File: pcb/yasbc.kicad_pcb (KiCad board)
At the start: 4 copper layers, 183 parts, among them J1 BOOT, J10 SSD1309, J2 USB TTY, J3 AudioJack3, J4 1V5, J5 3V3, J6 1V2, J7 USB DEV, J8 Micro_SD_Card, J9 USB HOST, Q1 AO3401A, Q2 AO3401A, SW1 RESET, SW2 SW_SPDT, SW3 SW_SPDT, SW4 SW_SPDT, SW5 SW_SPDT, SW6 SW_5WAY, U1 BCT2028, U2 ESP32-WROOM-32, U3 Allwinner_A13, U4 CH340E, U5 TD6810, U6 SE5120, U7 MT3608, U8 K4B4G1646E, U9 MPU-6050, Y1 24M

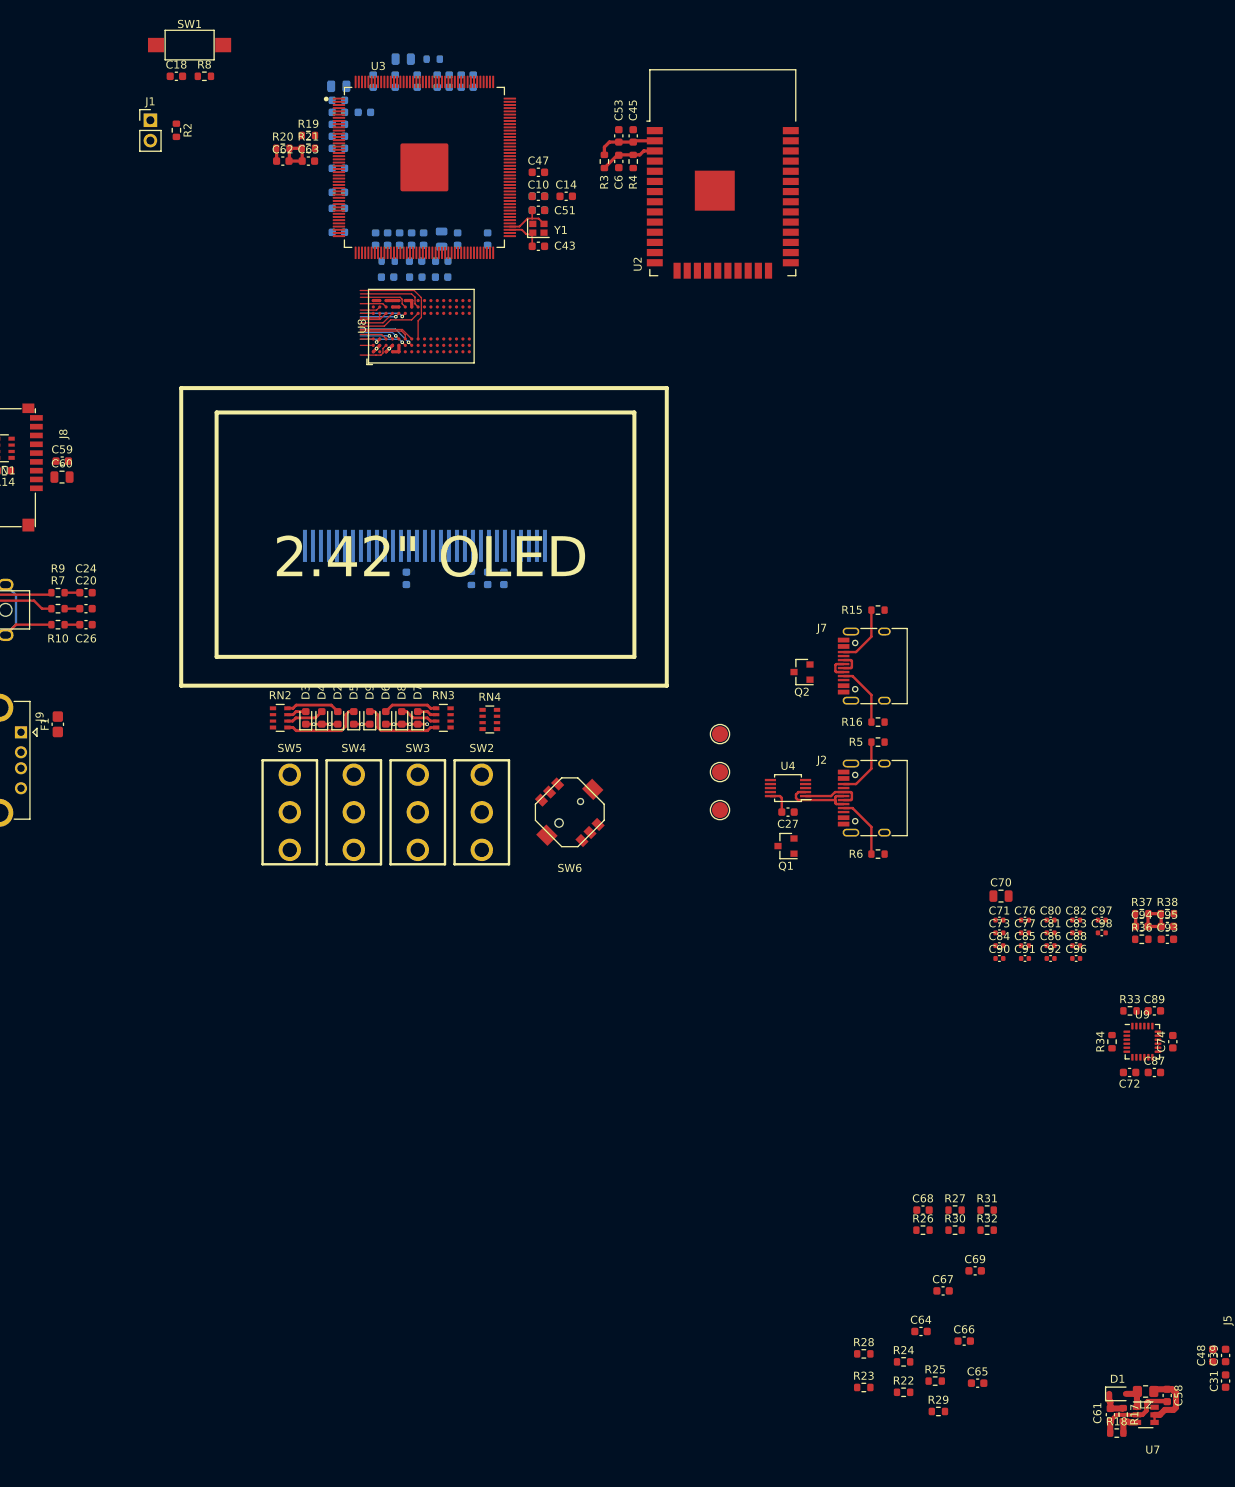
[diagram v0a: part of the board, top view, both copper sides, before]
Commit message: Removed OLED and ESP32
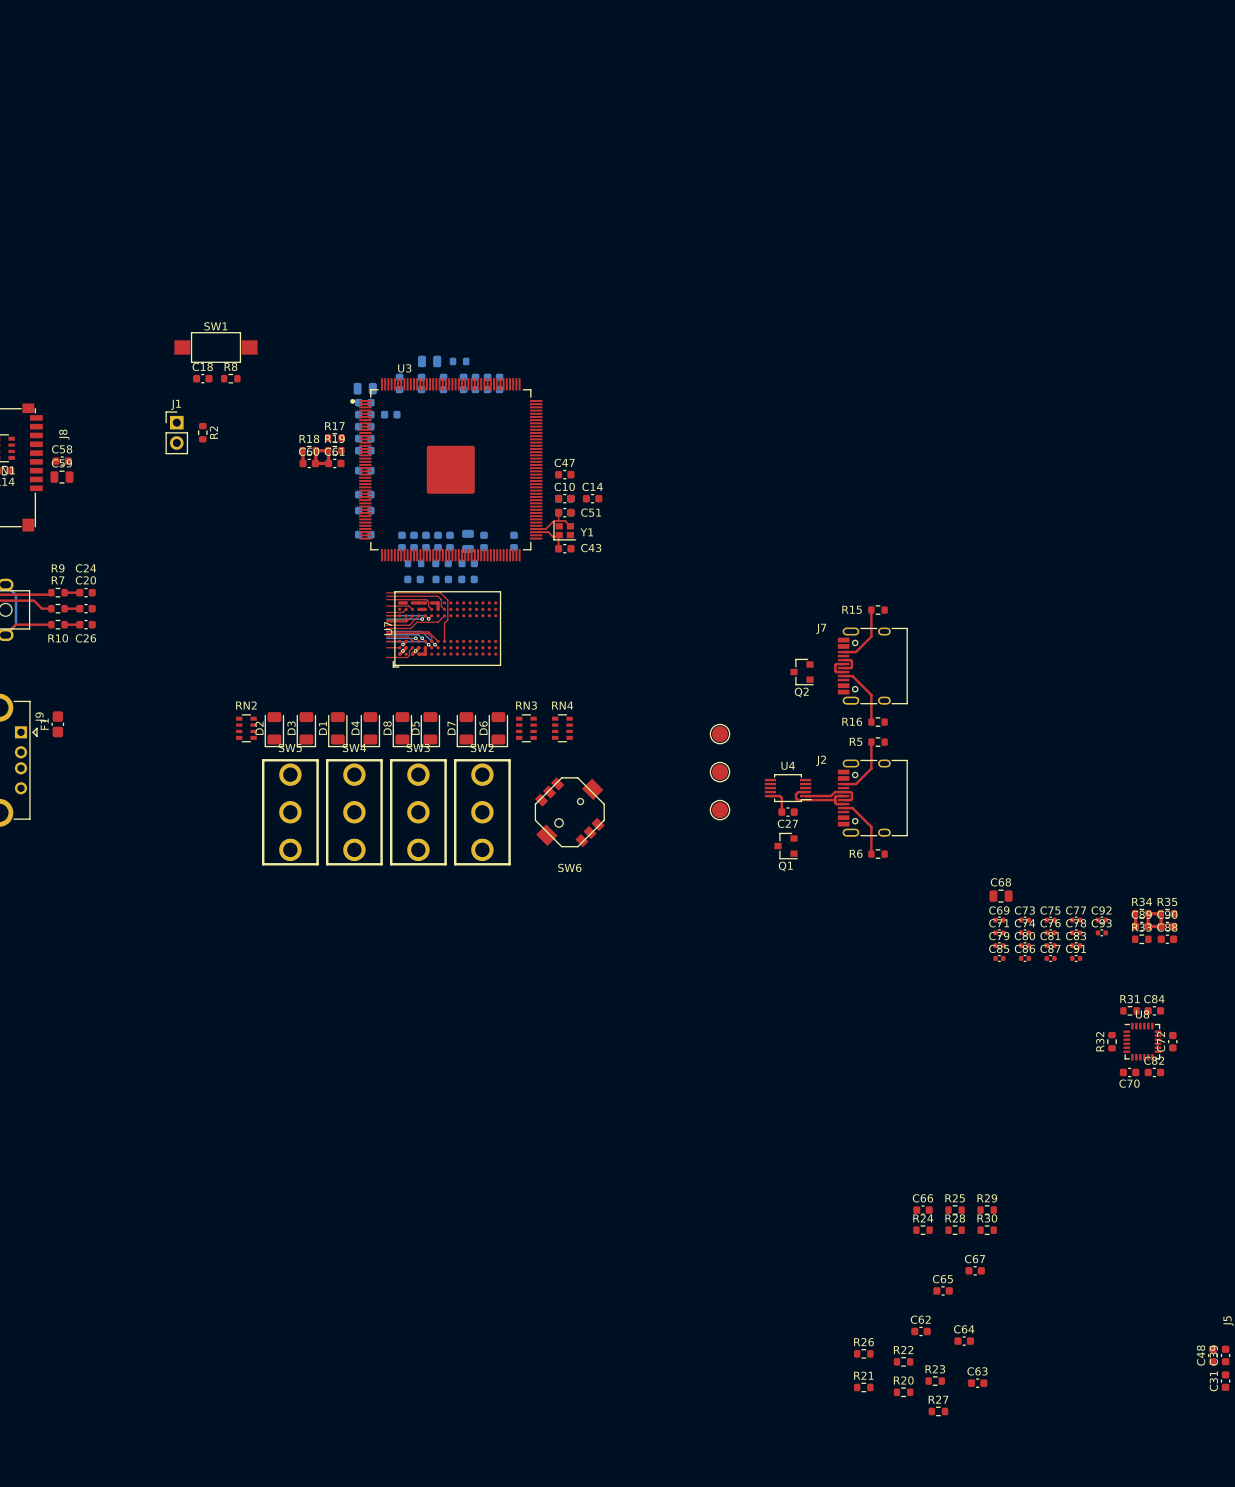
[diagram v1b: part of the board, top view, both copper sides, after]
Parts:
- removed C45: 0.1u, Capacitor_SMD:C_0603_1608Metric
- removed C53: 10u, Capacitor_SMD:C_0603_1608Metric
- removed the C58 at (205.1, 152.0)
- removed C6: DNF, Capacitor_SMD:C_0603_1608Metric
- removed the C61 at (198.0, 154.4)
- removed the C75 at (120.2, 49.9)
- removed the C78 at (122.2, 49.9)
- removed the C79 at (110.0, 49.9)
- removed the D1 at (198.9, 151.8)
- removed the D3 at (97.4, 67.3)
- removed J10: SSD1309, yasbc:SSD1309
- removed L2: 4.7u, Inductor_SMD:L_0805_2012Metric_Pad1.15x1.40mm_HandSolder
- removed the R17 at (199.6, 154.4)
- removed the R18 at (198.8, 156.7)
- removed R3: DNF, Resistor_SMD:R_0603_1608Metric
- removed the R35 at (118.1, 49.9)
- removed R4: 10K, Resistor_SMD:R_0603_1608Metric
- removed U2: ESP32-WROOM-32, RF_Module:ESP32-WROOM-32
- removed the U7 at (202.4, 154.4)
- added D2: LED_Small, LED_SMD:LED_1206_3216Metric, F.Cu at (93.5, 68.6)
- D1: renamed from D2; footprint LED_SMD:LED_0603_1608Metric -> LED_SMD:LED_1206_3216Metric
- D3: renamed from D4; footprint LED_SMD:LED_0603_1608Metric -> LED_SMD:LED_1206_3216Metric
- D4: renamed from D5; footprint LED_SMD:LED_0603_1608Metric -> LED_SMD:LED_1206_3216Metric
- D5: renamed from D6; footprint LED_SMD:LED_0603_1608Metric -> LED_SMD:LED_1206_3216Metric
- D6: renamed from D7; footprint LED_SMD:LED_0603_1608Metric -> LED_SMD:LED_1206_3216Metric
- D7: renamed from D8; footprint LED_SMD:LED_0603_1608Metric -> LED_SMD:LED_1206_3216Metric
- D8: renamed from D9; footprint LED_SMD:LED_0603_1608Metric -> LED_SMD:LED_1206_3216Metric
- moved U3 37.9 mm to (115.5, 36.3)
- moved C10 37.9 mm to (129.8, 39.9)
- moved C11 37.9 mm to (114.7, 25.5)
- moved C12 37.9 mm to (109.2, 25.5)
- moved C13 37.9 mm to (118.7, 25.5)
- moved C14 37.9 mm to (133.3, 39.9)
- moved C15 37.9 mm to (104.8, 29.4)
- moved C16 37.9 mm to (120.2, 25.5)
- moved C17 37.9 mm to (114.0, 45.2)
- moved C18 37.9 mm to (84.5, 24.9)
- moved C2 37.9 mm to (104.8, 26.1)
- moved C21 37.9 mm to (117.2, 25.5)
- moved C22 37.9 mm to (121.7, 25.5)
- moved C23 37.9 mm to (129.8, 41.6)
- moved C28 37.9 mm to (117.7, 48.0)
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- renumbered C59 to C58, C60 to C59, C62 to C60, C63 to C61, C64 to C62, C65 to C63, C66 to C64, C67 to C65, C68 to C66, C69 to C67, C70 to C68, C71 to C69, C72 to C70, C73 to C71, C74 to C72, C76 to C73, C77 to C74, C80 to C75, C81 to C76, C82 to C77, C83 to C78, C84 to C79, C85 to C80, C86 to C81, C87 to C82, C88 to C83, C89 to C84, C90 to C85, C91 to C86, C92 to C87, C93 to C88, C94 to C89, C95 to C90, C96 to C91, C97 to C92, C98 to C93, R19 to R17, R20 to R18, R21 to R19, R22 to R20, R23 to R21, R24 to R22, R25 to R23, R26 to R24, R27 to R25, R28 to R26, R29 to R27, R30 to R28, R31 to R29, R32 to R30, R33 to R31, R34 to R32, R36 to R33, R37 to R34, R38 to R35, U8 to U7, U9 to U8
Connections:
- U3 pad 1: /OLED_DC -> Net-(U3-Pad1)
- U3 pad 12: /ESP_RX -> Net-(U3-Pad12)
- U3 pad 13: /ESP_TX -> Net-(U3-Pad13)
- U3 pad 14: /ESP_RTS -> Net-(U3-Pad14)
- U3 pad 15: /ESP_CTS -> Net-(U3-Pad15)
- U3 pad 153: /ESP_EN -> Net-(U3-Pad153)
- U3 pad 162: /ESP_BOOT -> Net-(U3-Pad162)
- U3 pad 170: /ESP_DAT3 -> Net-(U3-Pad170)
- U3 pad 171: /ESP_DAT2 -> Net-(U3-Pad171)
- U3 pad 172: /ESP_DAT1 -> Net-(U3-Pad172)
- U3 pad 174: /ESP_DAT0 -> Net-(U3-Pad174)
- U3 pad 175: /ESP_CLK -> Net-(U3-Pad175)
- U3 pad 176: /ESP_CMD -> Net-(U3-Pad176)
- U3 pad 2: /OLED_RES -> Net-(U3-Pad2)
- U3 pad 3: /OLED_CS -> Net-(U3-Pad3)
- U3 pad 6: /OLED_SCLK -> Net-(U3-Pad6)
- U3 pad 8: /OLED_SDIN -> Net-(U3-Pad8)
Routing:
- net GND: track 44.1 -> 22.4 mm, vias 7 -> 1
- net Net-(D8-Pad2): track 10.4 -> 0.00 mm
- net Net-(D4-Pad2): track 10.3 -> 0.00 mm
- net VBUS: track 16.9 -> 8.00 mm
- net +3V3: track 10.9 -> 3.29 mm
- net /ESP_EN: track 7.19 -> 0.00 mm
- net Net-(D1-Pad2): track 6.80 -> 0.00 mm
- net Net-(D5-Pad2): track 6.80 -> 0.00 mm
- net Net-(D3-Pad2): track 4.79 -> 0.00 mm
- net Net-(D7-Pad2): track 4.79 -> 0.00 mm
- net Net-(D1-Pad2) (its old number): track 3.54 -> 0.00 mm
- net +12V: track 3.51 -> 0.00 mm
- net Net-(R17-Pad2): track 3.01 -> 0.00 mm
- net Net-(D2-Pad2): track 2.46 -> 0.00 mm
- net Net-(D6-Pad2): track 2.46 -> 0.00 mm
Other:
- board text removed: "2.42" OLED"

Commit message: Converted to kicad 6 and worked on pcb
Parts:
- added D9: 5V, Diode_SMD:D_SMB, F.Cu at (134.5, 143.4)
- added H1: MountingHole, MountingHole:MountingHole_3.2mm_M3, F.Cu at (132.5, -105.5)
- added H2: MountingHole, MountingHole:MountingHole_3.2mm_M3, F.Cu at (132.5, -14.5)
- added H3: MountingHole, MountingHole:MountingHole_3.2mm_M3, F.Cu at (41.5, -105.5)
- added H4: MountingHole, MountingHole:MountingHole_3.2mm_M3, F.Cu at (41.5, -14.5)
- added J10: Conn_02x20_Odd_Even, Connector_PinHeader_2.54mm:PinHeader_2x20_P2.54mm_Vertical, F.Cu at (47.0, -105.0)
- added R3: 5.1K, Resistor_SMD:R_0603_1608Metric, F.Cu at (159.6, 141.3)
- added R4: 5.1K, Resistor_SMD:R_0603_1608Metric, F.Cu at (163.6, 141.3)
- C10, C14, C47, C60, C61, R17, R18, R19: moved to B.Cu
- moved R6 226.2 mm to (12.6, -79.1), turned to 180 degrees
- moved J2 215.9 mm to (12.8, -72.1), turned to -90 degrees
- moved Q1 209.4 mm to (24.1, -78.1), turned to 0 degrees
- moved R5 206.9 mm to (12.6, -65.1), turned to 180 degrees
- moved U7 204.6 mm to (-51.6, -62.5), turned to 45 degrees
- moved C27 203.2 mm to (23.8, -73.8), turned to 180 degrees
- moved C23 199.8 mm to (-31.2, -76.6)
- moved U4 198.8 mm to (23.8, -70.8), turned to 0 degrees
- moved C14 198.0 mm to (-27.8, -75.3)
- moved C10 198.0 mm to (-31.3, -75.3)
- moved TP1 196.7 mm to (30.0, -77.7), turned to 0 degrees
- moved C47 194.9 mm to (-31.3, -72.9)
- moved C42 194.1 mm to (-27.8, -73.3), turned to 180 degrees
- moved R17 191.2 mm to (-53.9, -79.9), turned to -90 degrees
- moved R19 190.9 mm to (-52.2, -79.9), turned to -90 degrees
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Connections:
- U3 pad 10: /SW_RIGHT -> /SPI2_CS1
- U3 pad 103: /SW_UP -> Net-(U3-Pad103)
- U3 pad 104: /SW_LEFT -> Net-(U3-Pad104)
- U3 pad 105: /LED5 -> Net-(U3-Pad105)
- U3 pad 106: /LED6 -> Net-(U3-Pad106)
- U3 pad 114: Net-(U3-Pad114) -> /SPI2_CS0
- U3 pad 115: Net-(U3-Pad115) -> /SPI2_CLK
- U3 pad 116: Net-(U3-Pad116) -> /SPI2_MOSI
- U3 pad 117: Net-(U3-Pad117) -> /SPI2_MISO
- U3 pad 118: Net-(U3-Pad118) -> /SDC2_DAT0
- U3 pad 119: Net-(U3-Pad119) -> /SDC2_DAT1
- U3 pad 120: Net-(U3-Pad120) -> /SDC2_DAT2
- U3 pad 121: Net-(U3-Pad121) -> /SDC2_DAT3
- U3 pad 122: Net-(U3-Pad122) -> /SDC2_CMD
- U3 pad 123: Net-(U3-Pad123) -> /SDC2_CLK
- U3 pad 150: /SW_DOWN -> Net-(U3-Pad150)
- U3 pad 160: /LED8 -> Net-(U3-Pad160)
- U3 pad 161: /LED7 -> Net-(U3-Pad161)
- U3 pad 165: /LED4 -> /LED8
- U3 pad 166: /LED3 -> /LED7
- U3 pad 167: /LED2 -> /LED6
- U3 pad 168: /LED1 -> /LED5
- U3 pad 170: Net-(U3-Pad170) -> /LED4
- U3 pad 171: Net-(U3-Pad171) -> /LED3
- U3 pad 172: Net-(U3-Pad172) -> /LED2
- U3 pad 174: Net-(U3-Pad174) -> /LED1
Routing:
- net /DDR3_D4: track 13.4 -> 0.00 mm
- net /DDR3_DQS1-: track 2.97 -> 14.7 mm
- net /DDR3_DQS1+: track 3.56 -> 14.8 mm
- net /DDR3_CK-: track 0.00 -> 10.6 mm, vias 0 -> 2
- net /DDR3_DQS0+: track 6.35 -> 16.8 mm, vias 0 -> 2
- net /DDR3_CK+: track 0.00 -> 10.3 mm, vias 0 -> 2
- net /DDR3_DQS0-: track 6.93 -> 16.4 mm, vias 0 -> 2
- net /DDR3_D0: track 5.18 -> 14.5 mm
- net /DDR3_D6: track 7.28 -> 16.4 mm
- net /DDR3_D12: track 1.63 -> 10.7 mm
- net /DDR3_DM0: track 5.00 -> 13.7 mm, vias 1 -> 2
- net /DDR3_D8: track 4.55 -> 11.8 mm
- net /DDR3_D14: track 2.60 -> 8.94 mm
- net /DDR3_D2: track 5.95 -> 0.00 mm, vias 1 -> 0
- net /DDR3_D10: track 3.41 -> 8.44 mm
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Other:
- board outline added: 100 x 100 mm
- net class DDR3 removed
- net class Default removed
- board text added: "JLC2313 1.6mm"

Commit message: Routed DDR3 data signals
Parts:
- moved C10 119.4 mm to (86.0, -52.7)
- moved C11 119.4 mm to (80.7, -66.6)
- moved C12 119.4 mm to (75.2, -66.6)
- moved C13 119.4 mm to (84.7, -66.6)
- moved C16 119.4 mm to (86.2, -66.6)
- moved C21 119.4 mm to (83.2, -66.6)
- moved C22 119.4 mm to (87.7, -66.6)
- moved C23 119.4 mm to (86.1, -54.0)
- moved C42 119.4 mm to (89.5, -50.8)
- moved C43 119.4 mm to (94.8, -45.3)
- moved C47 119.4 mm to (86.0, -50.3)
- moved C50 119.4 mm to (77.9, -66.6)
- moved C51 119.4 mm to (96.9, -47.2)
- moved C55 119.4 mm to (78.9, -69.3)
- moved R11 119.4 mm to (82.7, -69.3)
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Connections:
- J10 pad 11: Net-(J10-Pad11) -> unconnected-(J10-Pad11)
- J10 pad 12: Net-(J10-Pad12) -> unconnected-(J10-Pad12)
- J10 pad 27: Net-(J10-Pad27) -> unconnected-(J10-Pad27)
- J10 pad 28: Net-(J10-Pad28) -> unconnected-(J10-Pad28)
- J10 pad 29: Net-(J10-Pad29) -> unconnected-(J10-Pad29)
- J10 pad 31: Net-(J10-Pad31) -> unconnected-(J10-Pad31)
- J10 pad 32: Net-(J10-Pad32) -> unconnected-(J10-Pad32)
- J10 pad 33: Net-(J10-Pad33) -> unconnected-(J10-Pad33)
- J10 pad 35: Net-(J10-Pad35) -> unconnected-(J10-Pad35)
- J10 pad 36: Net-(J10-Pad36) -> unconnected-(J10-Pad36)
- J10 pad 38: Net-(J10-Pad38) -> unconnected-(J10-Pad38)
- J10 pad 40: Net-(J10-Pad40) -> unconnected-(J10-Pad40)
- J10 pad 7: Net-(J10-Pad7) -> unconnected-(J10-Pad7)
- J2 pad A8: Net-(J2-PadA8) -> unconnected-(J2-PadA8)
- J2 pad B8: Net-(J2-PadB8) -> unconnected-(J2-PadB8)
- J7 pad A8: Net-(J7-PadA8) -> unconnected-(J7-PadA8)
- J7 pad B8: Net-(J7-PadB8) -> unconnected-(J7-PadB8)
- U3 pad 1: Net-(U3-Pad1) -> unconnected-(U3-Pad1)
- U3 pad 103: Net-(U3-Pad103) -> unconnected-(U3-Pad103)
- U3 pad 104: Net-(U3-Pad104) -> unconnected-(U3-Pad104)
- U3 pad 105: Net-(U3-Pad105) -> unconnected-(U3-Pad105)
- U3 pad 106: Net-(U3-Pad106) -> unconnected-(U3-Pad106)
- U3 pad 12: Net-(U3-Pad12) -> unconnected-(U3-Pad12)
- U3 pad 124: Net-(U3-Pad124) -> unconnected-(U3-Pad124)
- U3 pad 125: Net-(U3-Pad125) -> unconnected-(U3-Pad125)
- U3 pad 126: Net-(U3-Pad126) -> unconnected-(U3-Pad126)
- U3 pad 127: Net-(U3-Pad127) -> unconnected-(U3-Pad127)
- U3 pad 128: Net-(U3-Pad128) -> unconnected-(U3-Pad128)
- U3 pad 129: Net-(U3-Pad129) -> unconnected-(U3-Pad129)
- U3 pad 13: Net-(U3-Pad13) -> unconnected-(U3-Pad13)
- U3 pad 130: Net-(U3-Pad130) -> unconnected-(U3-Pad130)
- U3 pad 131: Net-(U3-Pad131) -> unconnected-(U3-Pad131)
- U3 pad 132: Net-(U3-Pad132) -> unconnected-(U3-Pad132)
- U3 pad 133: Net-(U3-Pad133) -> unconnected-(U3-Pad133)
- U3 pad 134: Net-(U3-Pad134) -> unconnected-(U3-Pad134)
- U3 pad 135: Net-(U3-Pad135) -> unconnected-(U3-Pad135)
- U3 pad 136: Net-(U3-Pad136) -> unconnected-(U3-Pad136)
- U3 pad 137: Net-(U3-Pad137) -> unconnected-(U3-Pad137)
- U3 pad 138: Net-(U3-Pad138) -> unconnected-(U3-Pad138)
- U3 pad 139: Net-(U3-Pad139) -> unconnected-(U3-Pad139)
- U3 pad 14: Net-(U3-Pad14) -> unconnected-(U3-Pad14)
- U3 pad 140: Net-(U3-Pad140) -> unconnected-(U3-Pad140)
- U3 pad 141: Net-(U3-Pad141) -> unconnected-(U3-Pad141)
- U3 pad 143: Net-(U3-Pad143) -> unconnected-(U3-Pad143)
- U3 pad 144: Net-(U3-Pad144) -> unconnected-(U3-Pad144)
- U3 pad 145: Net-(U3-Pad145) -> unconnected-(U3-Pad145)
- U3 pad 146: Net-(U3-Pad146) -> unconnected-(U3-Pad146)
- U3 pad 147: Net-(U3-Pad147) -> unconnected-(U3-Pad147)
- U3 pad 148: Net-(U3-Pad148) -> unconnected-(U3-Pad148)
- U3 pad 15: Net-(U3-Pad15) -> unconnected-(U3-Pad15)
- U3 pad 150: Net-(U3-Pad150) -> unconnected-(U3-Pad150)
- U3 pad 153: Net-(U3-Pad153) -> unconnected-(U3-Pad153)
- U3 pad 160: Net-(U3-Pad160) -> unconnected-(U3-Pad160)
- U3 pad 161: Net-(U3-Pad161) -> unconnected-(U3-Pad161)
- U3 pad 162: Net-(U3-Pad162) -> unconnected-(U3-Pad162)
- U3 pad 175: Net-(U3-Pad175) -> unconnected-(U3-Pad175)
- U3 pad 176: Net-(U3-Pad176) -> unconnected-(U3-Pad176)
- U3 pad 2: Net-(U3-Pad2) -> unconnected-(U3-Pad2)
- U3 pad 3: Net-(U3-Pad3) -> unconnected-(U3-Pad3)
- U3 pad 6: Net-(U3-Pad6) -> unconnected-(U3-Pad6)
- U3 pad 7: Net-(U3-Pad7) -> unconnected-(U3-Pad7)
- U3 pad 8: Net-(U3-Pad8) -> unconnected-(U3-Pad8)
- U3 pad 84: Net-(U3-Pad84) -> unconnected-(U3-Pad84)
- U3 pad 85: Net-(U3-Pad85) -> unconnected-(U3-Pad85)
- U3 pad 87: Net-(U3-Pad87) -> unconnected-(U3-Pad87)
- U3 pad 88: Net-(U3-Pad88) -> unconnected-(U3-Pad88)
- U3 pad 89: Net-(U3-Pad89) -> unconnected-(U3-Pad89)
- U3 pad 90: Net-(U3-Pad90) -> unconnected-(U3-Pad90)
- U3 pad 99: Net-(U3-Pad99) -> unconnected-(U3-Pad99)
- U4 pad 4: Net-(U4-Pad4) -> unconnected-(U4-Pad4)
- U4 pad 5: Net-(U4-Pad5) -> unconnected-(U4-Pad5)
- U4 pad 6: Net-(U4-Pad6) -> unconnected-(U4-Pad6)
- U7 pad A2: /DDR3_D13 -> /DDR3_D1
- U7 pad A3: /DDR3_D15 -> /DDR3_D3
- U7 pad A7: /DDR3_D12 -> /DDR3_D4
- U7 pad B7: /DDR3_DQS1- -> /DDR3_DQS0-
- U7 pad B8: /DDR3_D14 -> /DDR3_D6
- U7 pad C2: /DDR3_D11 -> /DDR3_D7
- U7 pad C3: /DDR3_D9 -> /DDR3_D5
- U7 pad C7: /DDR3_DQS1+ -> /DDR3_DQS0+
- U7 pad C8: /DDR3_D10 -> /DDR3_D2
- U7 pad D3: /DDR3_DM1 -> /DDR3_DM0
- U7 pad D7: /DDR3_D8 -> /DDR3_D0
- U7 pad E3: /DDR3_D0 -> /DDR3_D8
- U7 pad E7: /DDR3_DM0 -> /DDR3_DM1
- U7 pad F2: /DDR3_D2 -> /DDR3_D12
- U7 pad F3: /DDR3_DQS0+ -> /DDR3_DQS1+
- U7 pad F7: /DDR3_D1 -> /DDR3_D9
- U7 pad F8: /DDR3_D3 -> /DDR3_D11
- U7 pad G2: /DDR3_D6 -> /DDR3_D14
- U7 pad G3: /DDR3_DQS0- -> /DDR3_DQS1-
- U7 pad H3: /DDR3_D4 -> /DDR3_D10
- U7 pad H7: /DDR3_D7 -> /DDR3_D15
- U7 pad H8: /DDR3_D5 -> /DDR3_D13
- U7 pad J1: Net-(U7-PadJ1) -> unconnected-(U7-PadJ1)
- U7 pad J9: Net-(U7-PadJ9) -> unconnected-(U7-PadJ9)
- U7 pad L1: Net-(U7-PadL1) -> unconnected-(U7-PadL1)
- U7 pad L9: Net-(U7-PadL9) -> unconnected-(U7-PadL9)
- U7 pad M7: Net-(U7-PadM7) -> unconnected-(U7-PadM7)
- U8 pad 6: Net-(U8-Pad6) -> unconnected-(U8-Pad6)
- U8 pad 7: Net-(U8-Pad7) -> unconnected-(U8-Pad7)
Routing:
- net /DDR3_D4: track 0.00 -> 20.2 mm
- net /DDR3_D2: track 0.00 -> 20.1 mm
- net /DDR3_D15: track 0.00 -> 19.0 mm
- net /DDR3_D11: track 0.00 -> 18.9 mm
- net /DDR3_D13: track 0.00 -> 18.9 mm
- net /DDR3_D9: track 0.00 -> 18.9 mm
- net /DDR3_DM1: track 0.00 -> 15.9 mm, vias 0 -> 2
- net /DDR3_CK-: track 10.6 -> 0.00 mm, vias 2 -> 0
- net /DDR3_CK+: track 10.3 -> 0.00 mm, vias 2 -> 0
- net /DDR3_D5: track 7.19 -> 17.1 mm, vias 0 -> 2
- net /DDR3_D3: track 8.36 -> 17.1 mm, vias 0 -> 2
- net /DDR3_D7: track 8.99 -> 17.0 mm, vias 0 -> 2
- net /DDR3_D1: track 9.32 -> 17.0 mm, vias 0 -> 2
- net /DDR3_D10: track 8.44 -> 15.9 mm, vias 0 -> 2
- net /DDR3_D14: track 8.94 -> 15.9 mm, vias 0 -> 2
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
